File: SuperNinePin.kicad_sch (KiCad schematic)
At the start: 27 parts, among them J2 SNES, J3 Atari, Q1 2N3904, U2 74HC4040, U3 NE555P, U5 74HC595, U6 74HC595, U7 ULN2803A, U8 74HC74, U9 4051

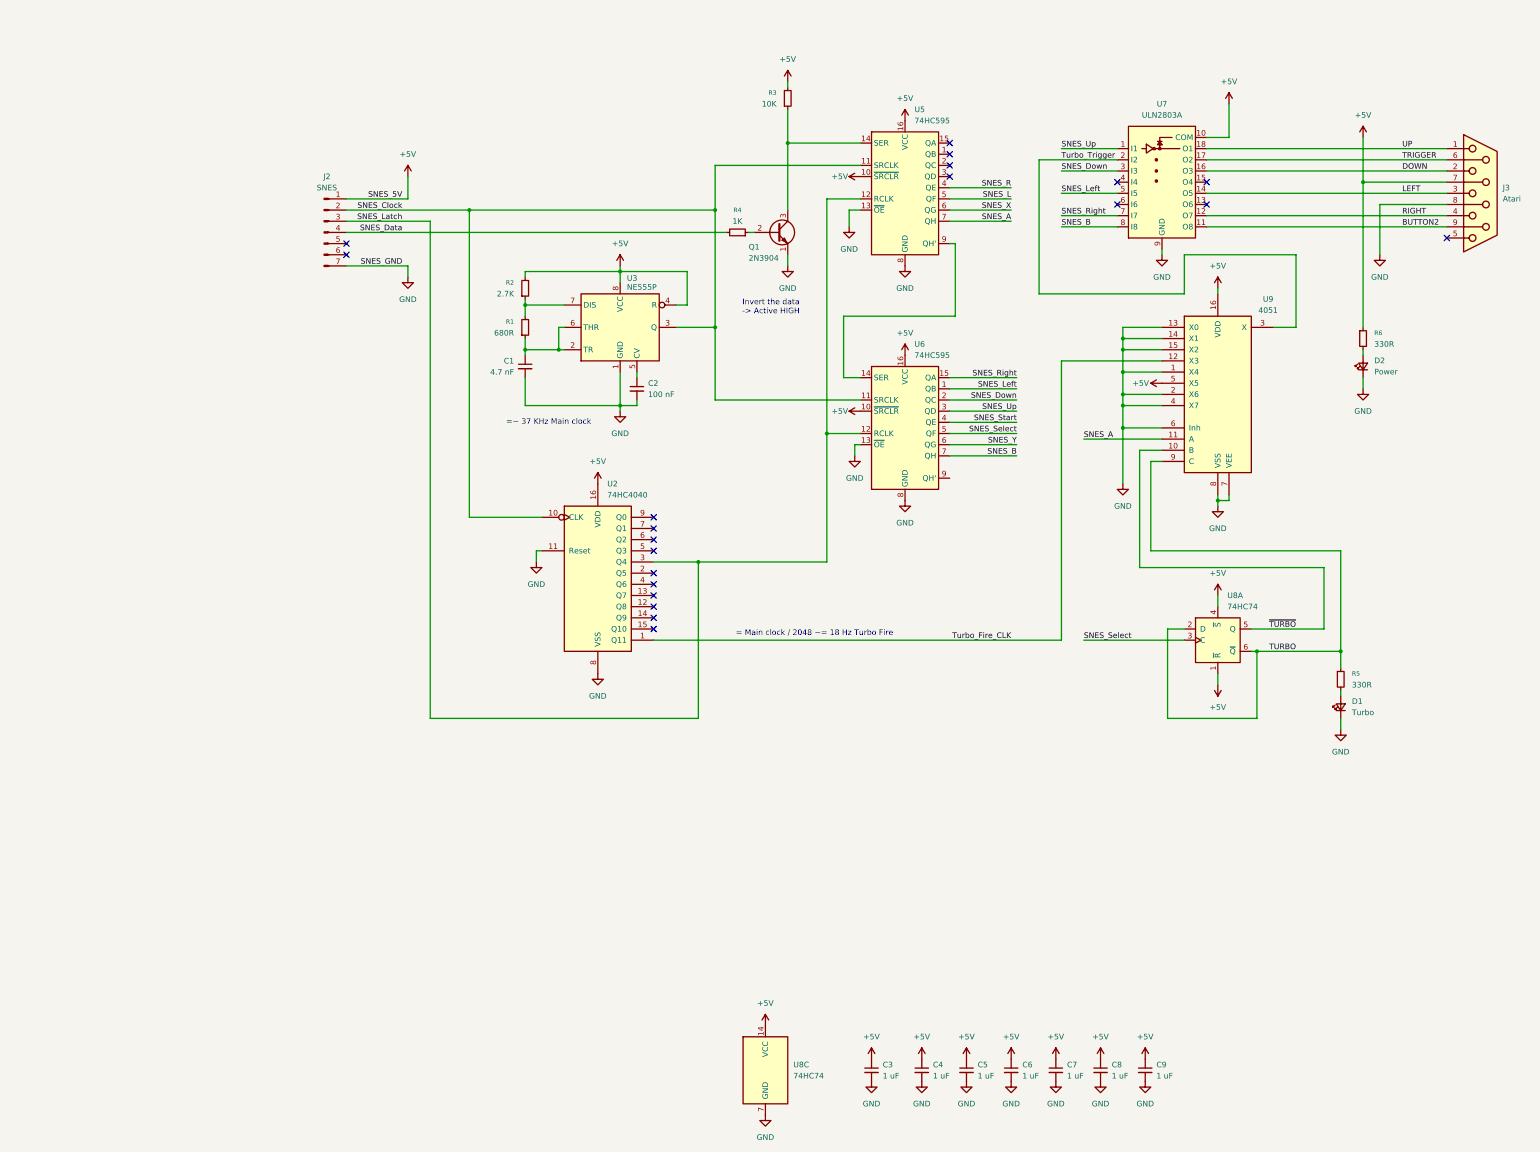
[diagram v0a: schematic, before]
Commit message: Swaps 555 + 4040 for 4060, swaps 74HC595 for TPIC6595
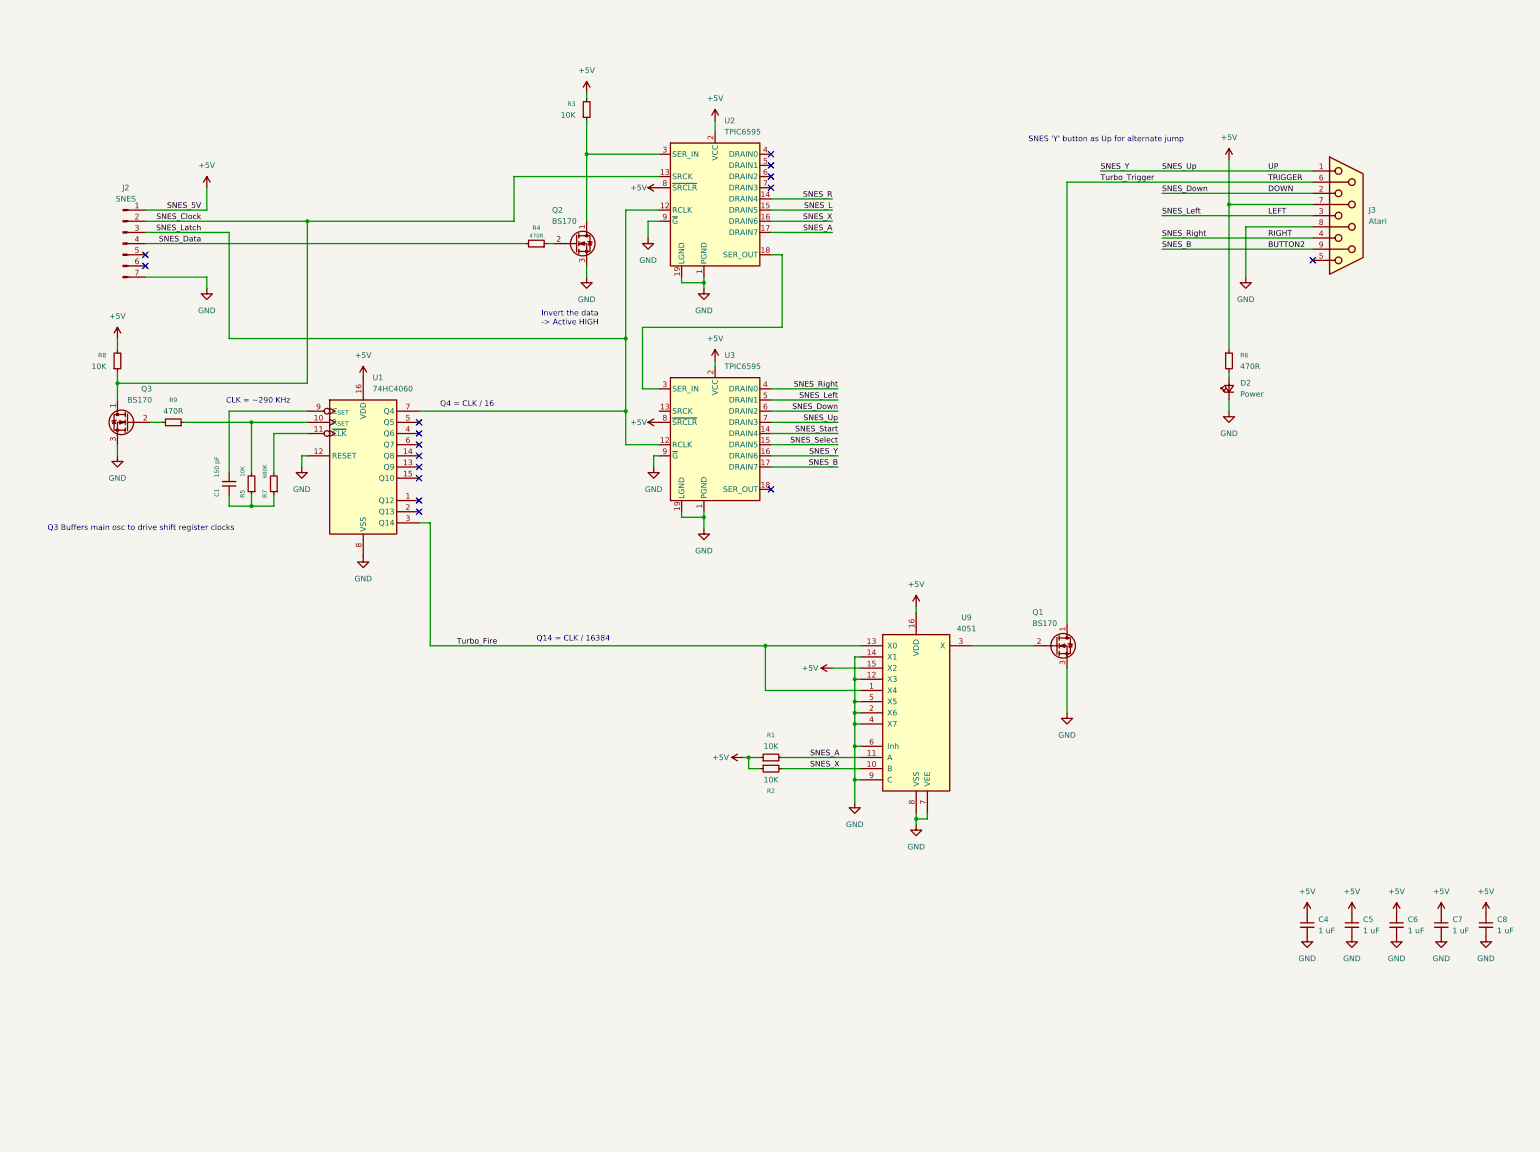
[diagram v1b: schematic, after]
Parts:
- removed C2: 100 nF, Capacitor_THT:C_Disc_D3.0mm_W1.6mm_P2.50mm, symbol Device:C_Small
- removed C3, C9: 1 uF, Capacitor_THT:C_Disc_D3.0mm_W1.6mm_P2.50mm, symbol Device:C_Small
- removed D1: Turbo, https://github.com/NovaSquirrel/NovaTheSquirrel?tab=readme-ov-file, symbol Device:LED_Small
- removed Q1: 2N3904, Package_TO_SOT_THT:TO-92_Inline_Wide, symbol Transistor_BJT:2N3904
- removed U2: 74HC4040, Package_DIP:DIP-16_W7.62mm, symbol 4xxx:4040
- removed U3: NE555P, Package_DIP:DIP-8_W7.62mm, symbol Timer:NE555P
- removed U5, U6: 74HC595, Package_DIP:DIP-16_W7.62mm, symbol 74xx:74HC595
- removed U7: ULN2803A, Package_DIP:DIP-18_W7.62mm, symbol Transistor_Array:ULN2803A
- removed U8: 74HC74, Package_DIP:DIP-14_W7.62mm, symbol 74xx:74HC74
- added Q1, Q2, Q3: BS170, Package_TO_SOT_THT:TO-92_Inline, symbol Transistor_FET:BS170
- added R7: 680K, Resistor_THT:R_Axial_DIN0207_L6.3mm_D2.5mm_P10.16mm_Horizontal, symbol Device:R_Small
- added R8: 10K, Resistor_THT:R_Axial_DIN0207_L6.3mm_D2.5mm_P10.16mm_Horizontal, symbol Device:R_Small
- added R9: 470R, Resistor_THT:R_Axial_DIN0207_L6.3mm_D2.5mm_P10.16mm_Horizontal, symbol Device:R_Small
- added U1: 74HC4060, symbol 74xx:74HC4060
- added U2, U3: TPIC6595, symbol Interface_Expansion:TPIC6595
- C1: value 4.7 nF -> 150 pF; footprint Capacitor_THT:C_Disc_D3.0mm_W1.6mm_P2.50mm -> (none)
- R1: value 680R -> 10K
- R2: value 2.7K -> 10K
- R4: value 1K -> 470R
- R5: value 330R -> 10K
- R6: value 330R -> 470R
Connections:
- net Turbo_Fire_CLK is gone; now on net GND: U9.12 (X3)
- net UP is gone; now on net SNES_Up: J3.1
- net ~{TURBO} is gone; now on net SNES_X: U9.10 (B)
- net +5V: now also R1.1, R2.1, U9.15 (X2), R8.2, U1.16 (VDD), U2.2 (VCC), U2.8 (~{SRCLR}), U3.2 (VCC), U3.8 (~{SRCLR}); no longer R2.2, U9.5 (X5)
- net BUTTON2: now also U3.17 (DRAIN7)
- net DOWN: now also U3.6 (DRAIN2)
- net GND: now also U9.5 (X5), U9.9 (C), Q1.3 (S), Q2.3 (S), Q3.3 (S), U1.12 (RESET), U1.8 (VSS), U2.1 (PGND), U2.10 (PGND), U2.11 (PGND), U2.19 (LGND), U2.20 (PGND), U2.9 (~{G}), U3.1 (PGND), U3.10 (PGND), U3.11 (PGND), U3.19 (LGND), U3.20 (PGND), U3.9 (~{G}); no longer C1.2, U9.1 (X4), U9.13 (X0), U9.15 (X2)
- net LEFT: now also U3.5 (DRAIN1)
- net RIGHT: now also U3.4 (DRAIN0)
- net SNES_A: now also R1.2, U2.17 (DRAIN7)
- net SNES_Clock: now also Q3.1 (D), R8.1, U2.13 (SRCK)
- net SNES_L: now also U2.15 (DRAIN5)
- net SNES_Latch: now also U1.7 (Q4), U2.12 (RCLK), U3.12 (RCLK)
- net SNES_R: now also U2.14 (DRAIN4)
- net SNES_Select: now also U3.15 (DRAIN5)
- net SNES_Start: now also U3.14 (DRAIN4)
- net SNES_Up: now also U3.16 (DRAIN6), U3.7 (DRAIN3)
- net SNES_X: now also R2.2, U2.16 (DRAIN6)
- net TRIGGER: now also Q1.1 (D)
- net at R5.2: now also R9.1, U1.10 (R_{SET})
- net at R3.1: now also Q2.1 (D), U2.3 (SER_IN)
- net at R4.1: now also Q2.2 (G)
- net at C1.1: now also R5.1, R7.1; no longer R1.1
- removed net TURBO: R5.1, U9.9 (C)
- net Turbo_Trigger: no longer names the net of U9.3 (X)
- net Turbo_Trigger: now also Q1.2 (G)
- new net: R7.2, U1.11 (~{CLK})
- new net: C1.2, U1.9 (C_{SET})
- new net: Q3.2 (G), R9.2
- new net: U2.18 (SER_OUT), U3.3 (SER_IN)
- new net Turbo_Fire: U1.3 (Q14), U9.1 (X4), U9.13 (X0)
- no-connect marks 21 -> 16
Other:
- note added: "CLK = ~290 KHz"
- note added: "Q14 = CLK / 16384"
- note added: "Q3 Buffers main osc to drive shift register clocks"
- note added: "Q4 = CLK / 16"
- note added: "SNES 'Y' button as Up for alternate jump"
- note removed: "= Main clock / 2048 ~= 18 Hz Turbo Fire"
- note removed: "=~ 37 KHz Main clock"
- moved on the sheet: C4, C5, C6, C7, C8, D2, J2, J3, R3, R4, R6, U9

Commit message: Adds gerbers, crude enclosure
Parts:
- removed C8: 1 uF, Capacitor_THT:C_Disc_D3.0mm_W1.6mm_P2.50mm, symbol Device:C_Small
- added C2: 10 µF, Capacitor_THT:C_Radial_D5.0mm_H5.0mm_P2.00mm, symbol Device:C_Polarized_Small
- added D1: FIRE, LED_THT:LED_D3.0mm, symbol Device:LED_Small
- added R10, R11, R12, R13, R14: 100R, Resistor_THT:R_Axial_DIN0207_L6.3mm_D2.5mm_P10.16mm_Horizontal, symbol Device:R_Small
- added R15: 470R, Resistor_THT:R_Axial_DIN0207_L6.3mm_D2.5mm_P10.16mm_Horizontal, symbol Device:R_Small
- C1: value 150 pF -> 68 pF; footprint (none) -> Capacitor_THT:C_Disc_D3.4mm_W2.1mm_P2.50mm
- J2: footprint (none) -> SuperNintendo:SNESController
- J3: footprint Connector_Dsub:DSUB-9_Socket_EdgeMount_P2.77mm -> Connector_Dsub:DSUB-9_Pins_Horizontal_P2.77x2.84mm_EdgePinOffset4.94mm_Housed_MountingHolesOffset4.94mm
- Q1, Q2, Q3: footprint Package_TO_SOT_THT:TO-92_Inline -> Package_TO_SOT_THT:TO-92_Inline_Wide
- R5: value 10K -> 1K
- R7: value 680K -> 100K
- R9: value 470R -> 100R
- U1: value 74HC4060 -> CD4060BE; footprint (none) -> Package_DIP:DIP-16_W7.62mm
- U2, U3: footprint (none) -> Package_DIP:DIP-20_W7.62mm
- U9: value 4051 -> CD4051
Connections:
- net +5V: now also C2.1, D1.2 (A)
- net BUTTON2: now also R14.2; no longer U3.17 (DRAIN7)
- net DOWN: now also R11.2; no longer U3.6 (DRAIN2)
- net GND: now also U9.1 (X4), C2.2; no longer U9.14 (X1)
- net LEFT: now also R12.2; no longer U3.5 (DRAIN1)
- net RIGHT: now also R13.2; no longer U3.4 (DRAIN0)
- net SNES_Clock: now also U3.13 (SRCK)
- net SNES_Latch: now also U1.5 (Q5); no longer U1.7 (Q4)
- net SNES_Up: now also R9.1; no longer J3.1
- net Turbo_Fire: now also U9.14 (X1); no longer U9.1 (X4)
- net at R5.2, U1.10 (R_{SET}): now also Q3.2 (G); no longer R9.1
- net UP: now reaches R9.2
- net UP: now also J3.1; no longer Q3.2 (G)
- net TRIGGER renamed BUTTON1
- net BUTTON1: now also R10.2; no longer Q1.1 (D)
- new net: D1.1 (K), R15.1
- new net SNES_B: R14.1, U3.17 (DRAIN7)
- new net SNES_Down: R11.1, U3.6 (DRAIN2)
- new net SNES_Left: R12.1, U3.5 (DRAIN1)
- new net SNES_Right: R13.1, U3.4 (DRAIN0)
- new net Turbo_Trigger: Q1.1 (D), R10.1, R15.2
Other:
- note added: "Q5 = CLK / 32"
- note removed: "Q4 = CLK / 16"
- moved on the sheet: C1, C4, C5, C6, C7, D2, J2, J3, Q1, Q2, Q3, R1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
